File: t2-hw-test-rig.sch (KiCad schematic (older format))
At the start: 0 parts

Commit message: added the SAM and some power-related things
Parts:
- added C? (x8): TM_C, symbol TM_C
- added L?: TM_L, symbol TM_L
- added R? (x2): TM_R, symbol TM_R
- added U?: SAMD21G14A-MU, QFN48, symbol SAMD21G14A-MU
- added U?: MAX6106, symbol MAX6106
- added U?: AP3418, symbol AP3418
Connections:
- net labels added: GND
- wire segments 0 -> 34

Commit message: put at least one of most of the critical components onto the schematic
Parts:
- added CON?: BARREL_JACK, symbol BARREL_JACK
- added J?: USB_A_2_stack, symbol USB_A_2_stack
- added J?: MICROUSB-TH, symbol MICROUSB-TH
- added J? (x2): MODULE_HEADER, symbol MODULE_HEADER
- added Q?: nMOS, symbol nMOS
- added U?: FE1.1, symbol FE1.1
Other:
- moved on the sheet: U?
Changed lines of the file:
@@
 L SAMD21G14A-MU U?
 U 1 1 55305B30
-P 4900 5500
-F 0 "U?" H 3750 7150 40  0000 C CNN
-F 1 "SAMD21G14A-MU" H 4900 5500 40  0000 C CNN
-F 2 "QFN48" H 4900 5400 32  0000 C CIN
-F 3 "" H 3700 5050 60  0000 C CNN
-	1    4900 5500
+P 4000 3600
+F 0 "U?" H 2850 5250 40  0000 C CNN
+F 1 "SAMD21G14A-MU" H 4000 3600 40  0000 C CNN
+F 2 "QFN48" H 4000 3500 32  0000 C CIN
+F 3 "" H 2800 3150 60  0000 C CNN
+	1    4000 3600
 	1    0    0    -1
 $EndComp
@@
 	9800 6500 9900 6500
 Connection ~ 9400 6300
+$Comp
+L FE1.1 U?
+U 1 1 55308B37
+P 4000 8200
+F 0 "U?" H 2900 9650 60  0000 C CNN
+F 1 "FE1.1" H 4000 8250 60  0000 C CNN
+F 2 "" H 4000 8500 60  0000 C CNN
+F 3 "" H 4000 8500 60  0000 C CNN
+	1    4000 8200
+	1    0    0    -1
+$EndComp
+$Comp
+L BARREL_JACK CON?
+U 1 1 553094E6
+P 6600 1400
+F 0 "CON?" H 6600 1650 60  0000 C CNN
+F 1 "BARREL_JACK" H 6600 1200 60  0000 C CNN
+F 2 "" H 6600 1400 60  0000 C CNN
+F 3 "" H 6600 1400 60  0000 C CNN
+	1    6600 1400
+	-1   0    0    -1
+$EndComp
+$Comp
+L USB_A_2_stack J?
+U 1 1 55309695
+P 8500 2300
+F 0 "J?" H 7900 2850 60  0000 C CNN
+F 1 "USB_A_2_stack" H 8500 2300 60  0000 C CNN
+F 2 "" H 9100 2800 60  0000 C CNN
+F 3 "" H 9100 2800 60  0000 C CNN
+	1    8500 2300
+	1    0    0    -1
+$EndComp
+$Comp
+L nMOS Q?
+U 1 1 55309A7F
+P 7400 3450
+F 0 "Q?" H 7400 3301 40  0000 R CNN
+F 1 "nMOS" H 7400 3600 40  0000 R CNN
+F 2 "" H 7270 3552 29  0000 C CNN
+F 3 "" H 7400 3450 60  0000 C CNN
+	1    7400 3450
+	1    0    0    -1
+$EndComp
+$Comp
+L MICROUSB-TH J?
+U 1 1 55309B7E
+P 7900 4200
+F 0 "J?" H 7500 4550 60  0000 C CNN
+F 1 "MICROUSB-TH" V 7750 4150 60  0000 C CNN
+F 2 "" H 7900 4200 60  0000 C CNN
+F 3 "" H 7900 4200 60  0000 C CNN
+	1    7900 4200
+	1    0    0    -1
+$EndComp
+$Comp
+L MODULE_HEADER J?
+U 1 1 55309C17
+P 6600 5300
+F 0 "J?" H 6250 5850 60  0000 C CNN
+F 1 "MODULE_HEADER" V 6300 5250 60  0000 C CNN
+F 2 "" H 6600 5300 60  0000 C CNN
+F 3 "" H 6600 5300 60  0000 C CNN
+	1    6600 5300
+	1    0    0    -1
+$EndComp
+$Comp
+L MODULE_HEADER J?
+U 1 1 55309F9E
+P 6600 6600
+F 0 "J?" H 6250 7150 60  0000 C CNN
+F 1 "MODULE_HEADER" V 6300 6550 60  0000 C CNN
+F 2 "" H 6600 6600 60  0000 C CNN
+F 3 "" H 6600 6600 60  0000 C CNN
+	1    6600 6600
+	1    0    0    -1
+$EndComp
 $EndSCHEMATC

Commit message: added current sense amplifier
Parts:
- removed U?: MAX6106, symbol MAX6106
- added U?: MAX6102, symbol MAX6102
- added U?: MAX9919, symbol MAX9919
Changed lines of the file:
@@
-$EndComp
-$Comp
-L MAX6106 U?
-U 1 1 5530666E
-P 10400 6400
-F 0 "U?" H 10200 6650 60  0000 C CNN
-F 1 "MAX6106" H 10400 6400 60  0000 C CNN
-F 2 "" H 10400 6400 60  0000 C CNN
-F 3 "" H 10400 6400 60  0000 C CNN
-	1    10400 6400
-	1    0    0    -1
 $EndComp
 $Comp
@@
 	1    0    0    -1
 $EndComp
+$Comp
+L MAX6102 U?
+U 1 1 5530AB65
+P 10400 6400
+F 0 "U?" H 10200 6650 60  0000 C CNN
+F 1 "MAX6102" H 10400 6400 60  0000 C CNN
+F 2 "" H 10400 6400 60  0000 C CNN
+F 3 "" H 10400 6400 60  0000 C CNN
+	1    10400 6400
+	1    0    0    -1
+$EndComp
+$Comp
+L MAX9919 U?
+U 1 1 5530BA79
+P 11600 1700
+F 0 "U?" H 11300 2350 60  0000 C CNN
+F 1 "MAX9919" H 11600 1700 60  0000 C CNN
+F 2 "" H 11600 1700 60  0000 C CNN
+F 3 "" H 11600 1700 60  0000 C CNN
+	1    11600 1700
+	1    0    0    -1
+$EndComp

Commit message: CSA support circuitry
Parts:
- added C? (x2): 100nF, symbol TM_C
- added L?: TM_L, symbol TM_L
- added R?: TM_R, symbol TM_R
- U?: value MAX9919 -> MAX9919FASA+
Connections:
- net labels added: +5V
- wire segments 34 -> 73
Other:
- moved on the sheet: C?, L?, Q?, R?, U?

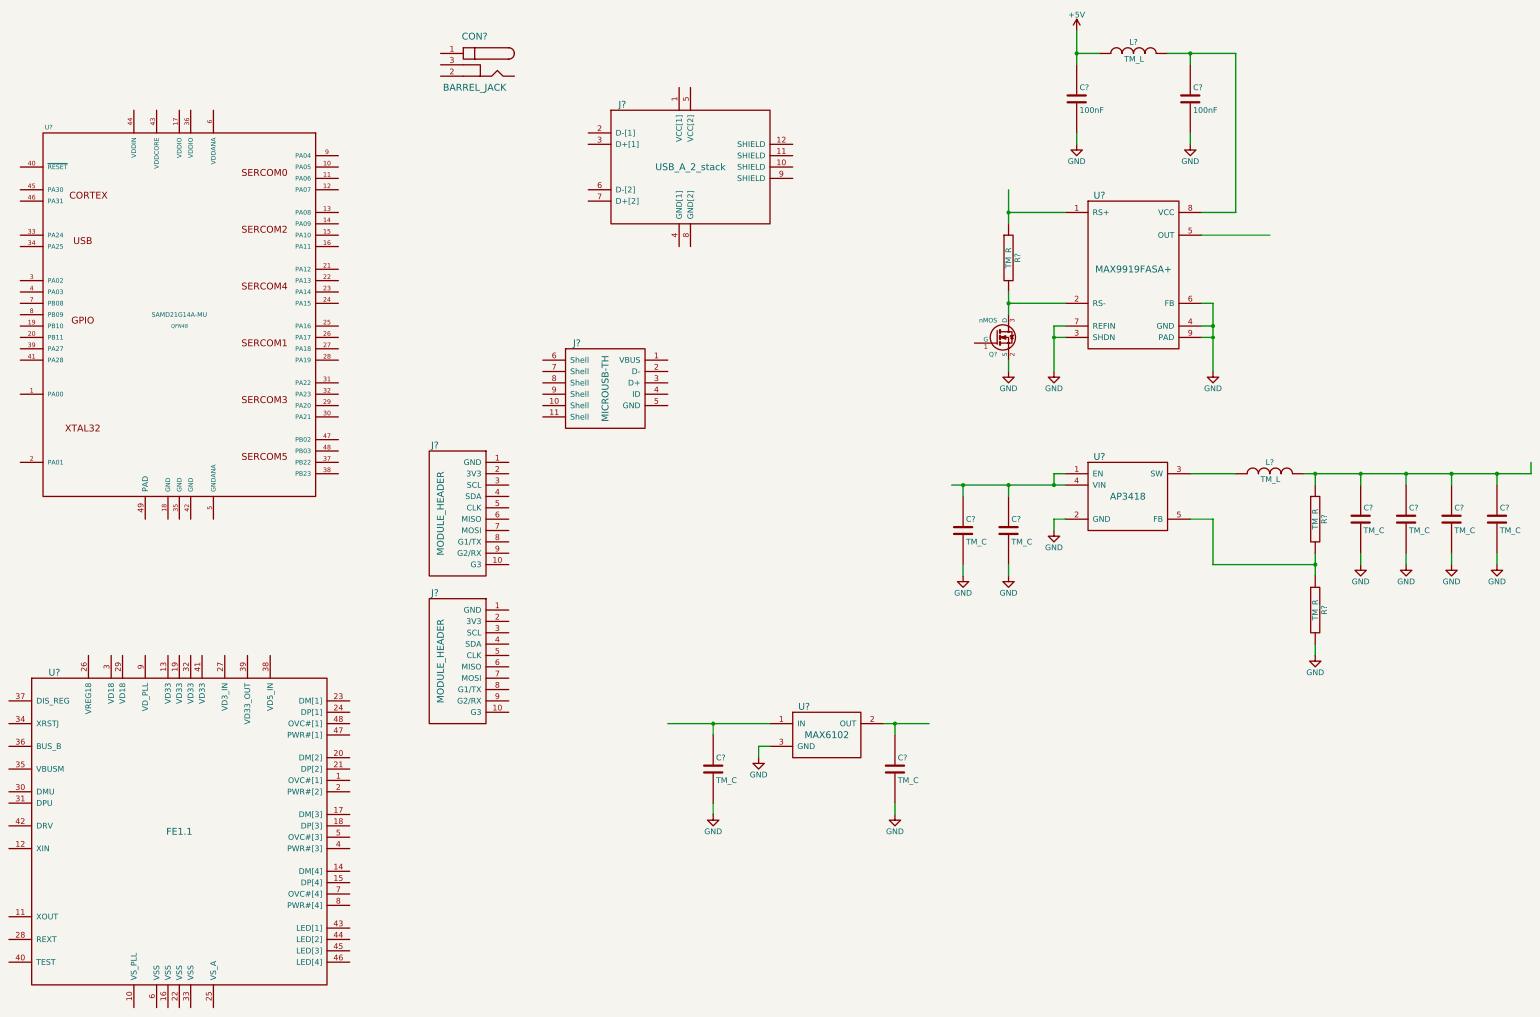
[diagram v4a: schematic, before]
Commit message: swapped switcher for an ldo
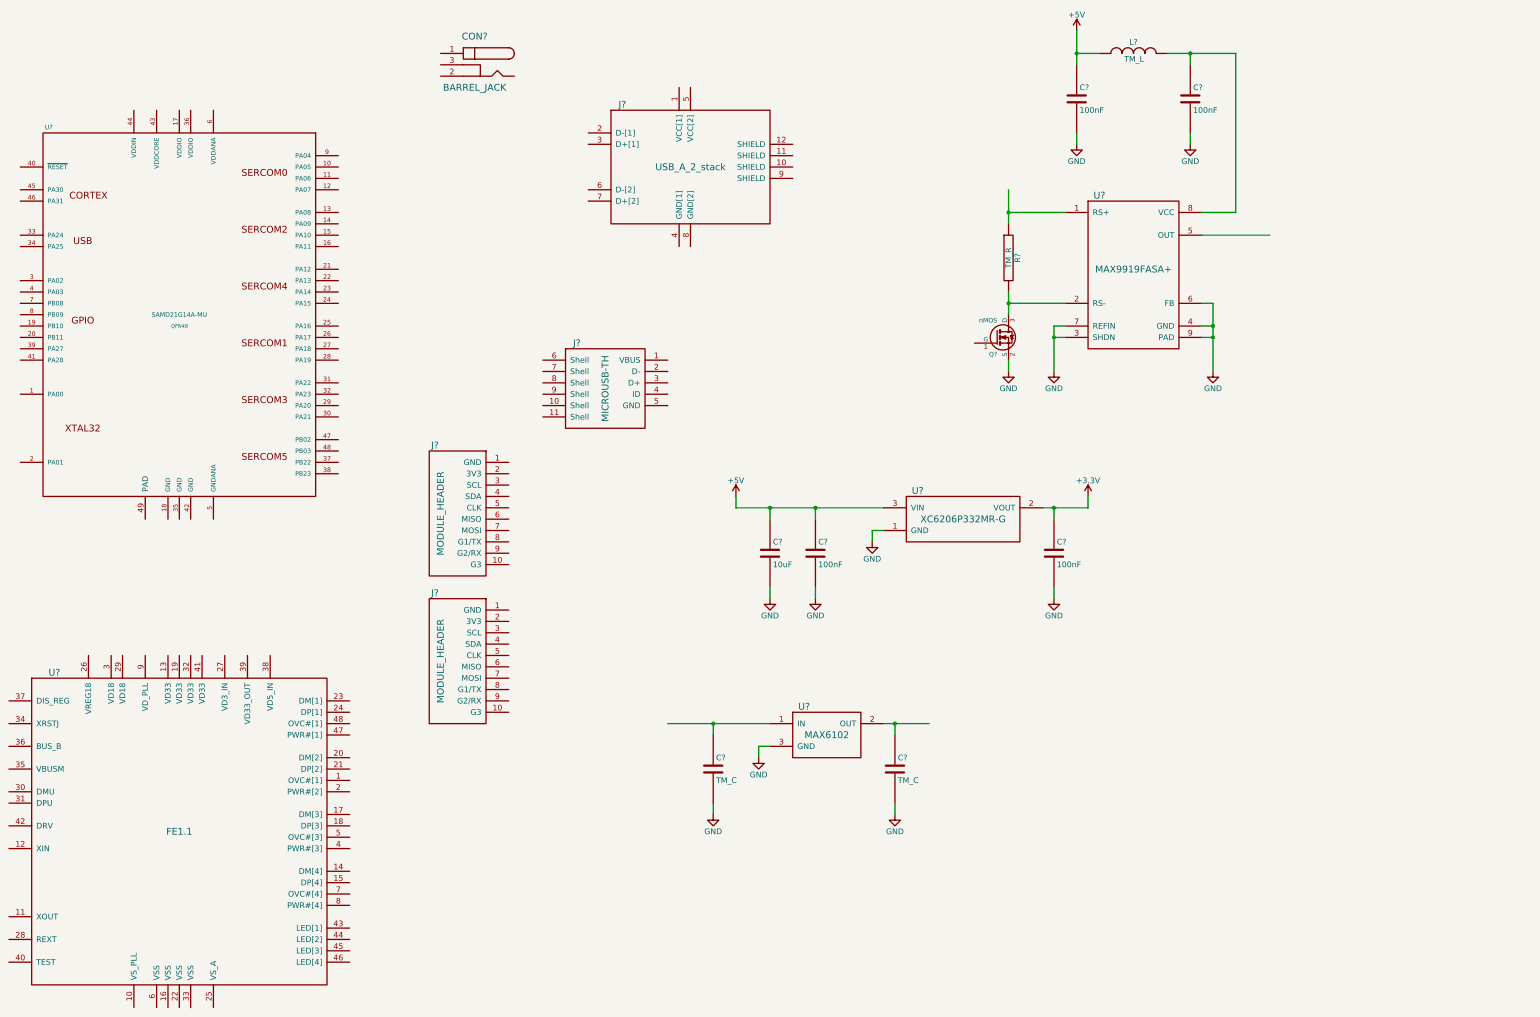
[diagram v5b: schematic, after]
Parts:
- removed C? (x6): TM_C, symbol TM_C
- removed L?: TM_L, symbol TM_L
- removed R? (x2): TM_R, symbol TM_R
- removed U?: AP3418, symbol AP3418
- added C? (x2): 100nF, symbol TM_C
- added C?: 10uF, symbol TM_C
- added U?: XC6206P332MR-G, symbol XC6206
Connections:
- net labels added: +3.3V
- wire segments 73 -> 41

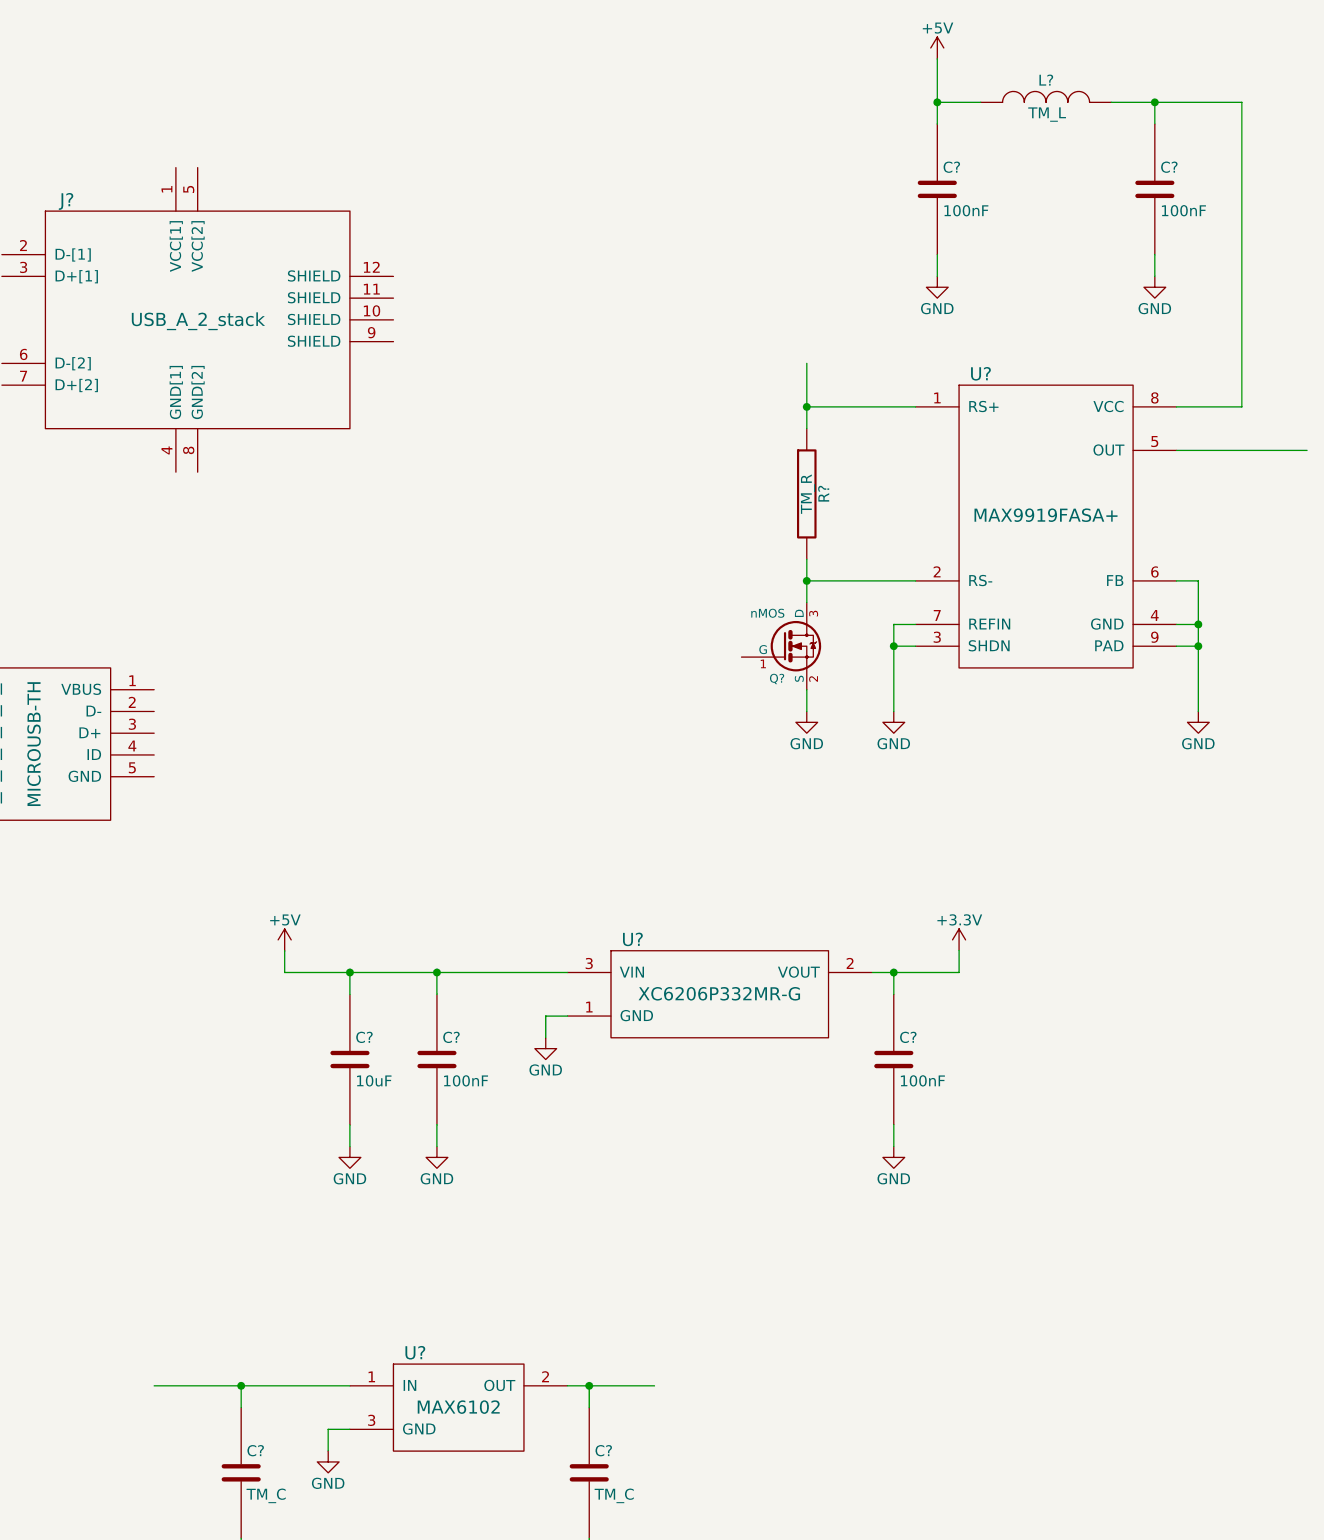
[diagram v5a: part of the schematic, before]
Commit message: picked an nmos
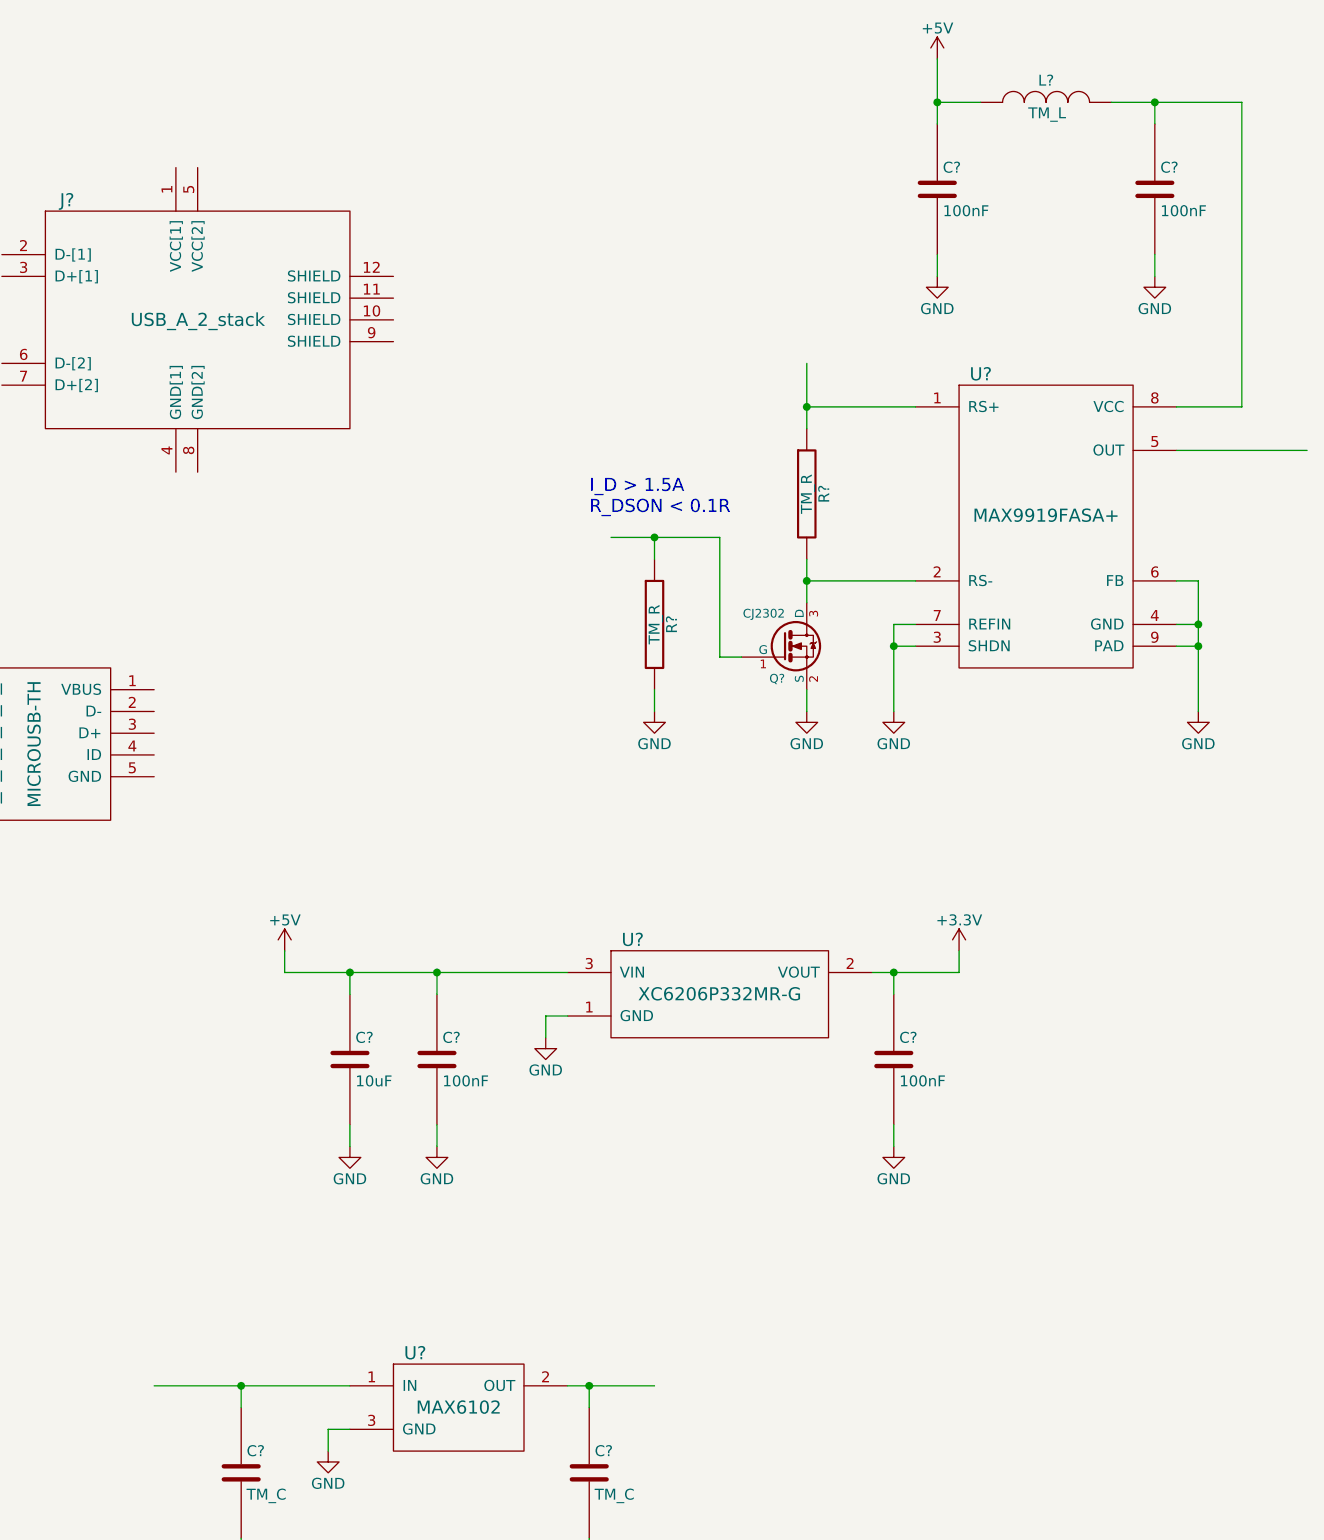
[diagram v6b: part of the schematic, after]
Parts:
- added R?: TM_R, symbol TM_R
- Q?: value nMOS -> CJ2302
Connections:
- wire segments 41 -> 59
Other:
- note added: "I_D > 1.5A\nR_DSON < 0.1R"
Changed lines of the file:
@@
 	8700 7200 8700 7300
 Wire Wire Line
-	10200 7200 10600 7200
+	10200 7200 10300 7200
+Wire Wire Line
+	10300 7200 10600 7200
 Connection ~ 10300 7200
 Wire Wire Line
-	8300 7200 9200 7200
+	8300 7200 8700 7200
+Wire Wire Line
+	8700 7200 9200 7200
 $Comp
 L GND #PWR?
@@
 P 11200 3800
 F 0 "Q?" H 11200 3651 40  0000 R CNN
-F 1 "nMOS" H 11200 3950 40  0000 R CNN
+F 1 "CJ2302" H 11200 3950 40  0000 R CNN
 F 2 "" H 11070 3902 29  0000 C CNN
-F 3 "" H 11200 3800 60  0000 C CNN
+F 3 "http://www.seeedstudio.com/wiki/images/e/e7/0440200P1.pdf" H 11200 3800 60  0001 C CNN
 	1    11200 3800
 	1    0    0    -1
@@
 	11800 3500 11300 3500
 Wire Wire Line
-	11300 3400 11300 3600
+	11300 3400 11300 3500
+Wire Wire Line
+	11300 3500 11300 3600
 Wire Wire Line
 	11300 2700 11800 2700
 Wire Wire Line
-	11300 2500 11300 2800
+	11300 2500 11300 2700
+Wire Wire Line
+	11300 2700 11300 2800
 $Comp
 L TM_C C?
@@
 $EndComp
 Wire Wire Line
-	13100 3500 13100 4100
+	13100 3500 13100 3700
+Wire Wire Line
+	13100 3700 13100 3800
+Wire Wire Line
+	13100 3800 13100 4100
 Wire Wire Line
 	13000 3700 13100 3700
@@
 	11800 3700 11700 3700
 Wire Wire Line
-	11700 3700 11700 4100
+	11700 3700 11700 3800
+Wire Wire Line
+	11700 3800 11700 4100
 Wire Wire Line
 	11800 3800 11700 3800
@@
 $EndComp
 Wire Wire Line
-	11900 1100 11900 1400
+	11900 1100 11900 1300
+Wire Wire Line
+	11900 1300 11900 1400
 $Comp
 L TM_C C?
@@
 	12900 2100 12900 2000
 Wire Wire Line
-	12700 1300 13300 1300
+	12700 1300 12900 1300
+Wire Wire Line
+	12900 1300 13300 1300
 Connection ~ 12900 1300
 Connection ~ 11300 3500
@@
 $EndComp
 Wire Wire Line
-	8900 5300 10200 5300
+	8900 5300 9200 5300
+Wire Wire Line
+	9200 5300 9600 5300
+Wire Wire Line
+	9600 5300 10200 5300
 Wire Wire Line
 	8900 5300 8900 5200
 Wire Wire Line
-	11600 5300 12000 5300
+	11600 5300 11700 5300
+Wire Wire Line
+	11700 5300 12000 5300
 $Comp
 L GND #PWR?
@@
 Wire Wire Line
 	12000 5300 12000 5200
+Text Notes 10300 3200 0    60   ~ 0
+I_D > 1.5A\nR_DSON < 0.1R
+Wire Wire Line
+	11000 3850 10900 3850
+Wire Wire Line
+	10900 3850 10900 3300
+Wire Wire Line
+	10900 3300 10600 3300
+Wire Wire Line
+	10600 3300 10400 3300
+$Comp
+L TM_R R?
+U 1 1 55314987
+P 10600 3700
+F 0 "R?" V 10680 3700 50  0000 C CNN
+F 1 "TM_R" V 10600 3700 50  0000 C CNN
+F 2 "" V 10530 3700 30  0000 C CNN
+F 3 "" H 10600 3700 30  0000 C CNN
+	1    10600 3700
+	1    0    0    -1
+$EndComp
+Wire Wire Line
+	10600 3400 10600 3300
+Connection ~ 10600 3300
+Wire Wire Line
+	10600 4000 10600 4100
+$Comp
+L GND #PWR?
+U 1 1 55314A47
+P 10600 4100
+F 0 "#PWR?" H 10600 3850 50  0001 C CNN
+F 1 "GND" H 10600 3950 50  0000 C CNN
+F 2 "" H 10600 4100 60  0000 C CNN
+F 3 "" H 10600 4100 60  0000 C CNN
+	1    10600 4100
+	1    0    0    -1
+$EndComp
 $EndSCHEMATC
